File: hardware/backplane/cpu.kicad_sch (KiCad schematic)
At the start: 0 parts

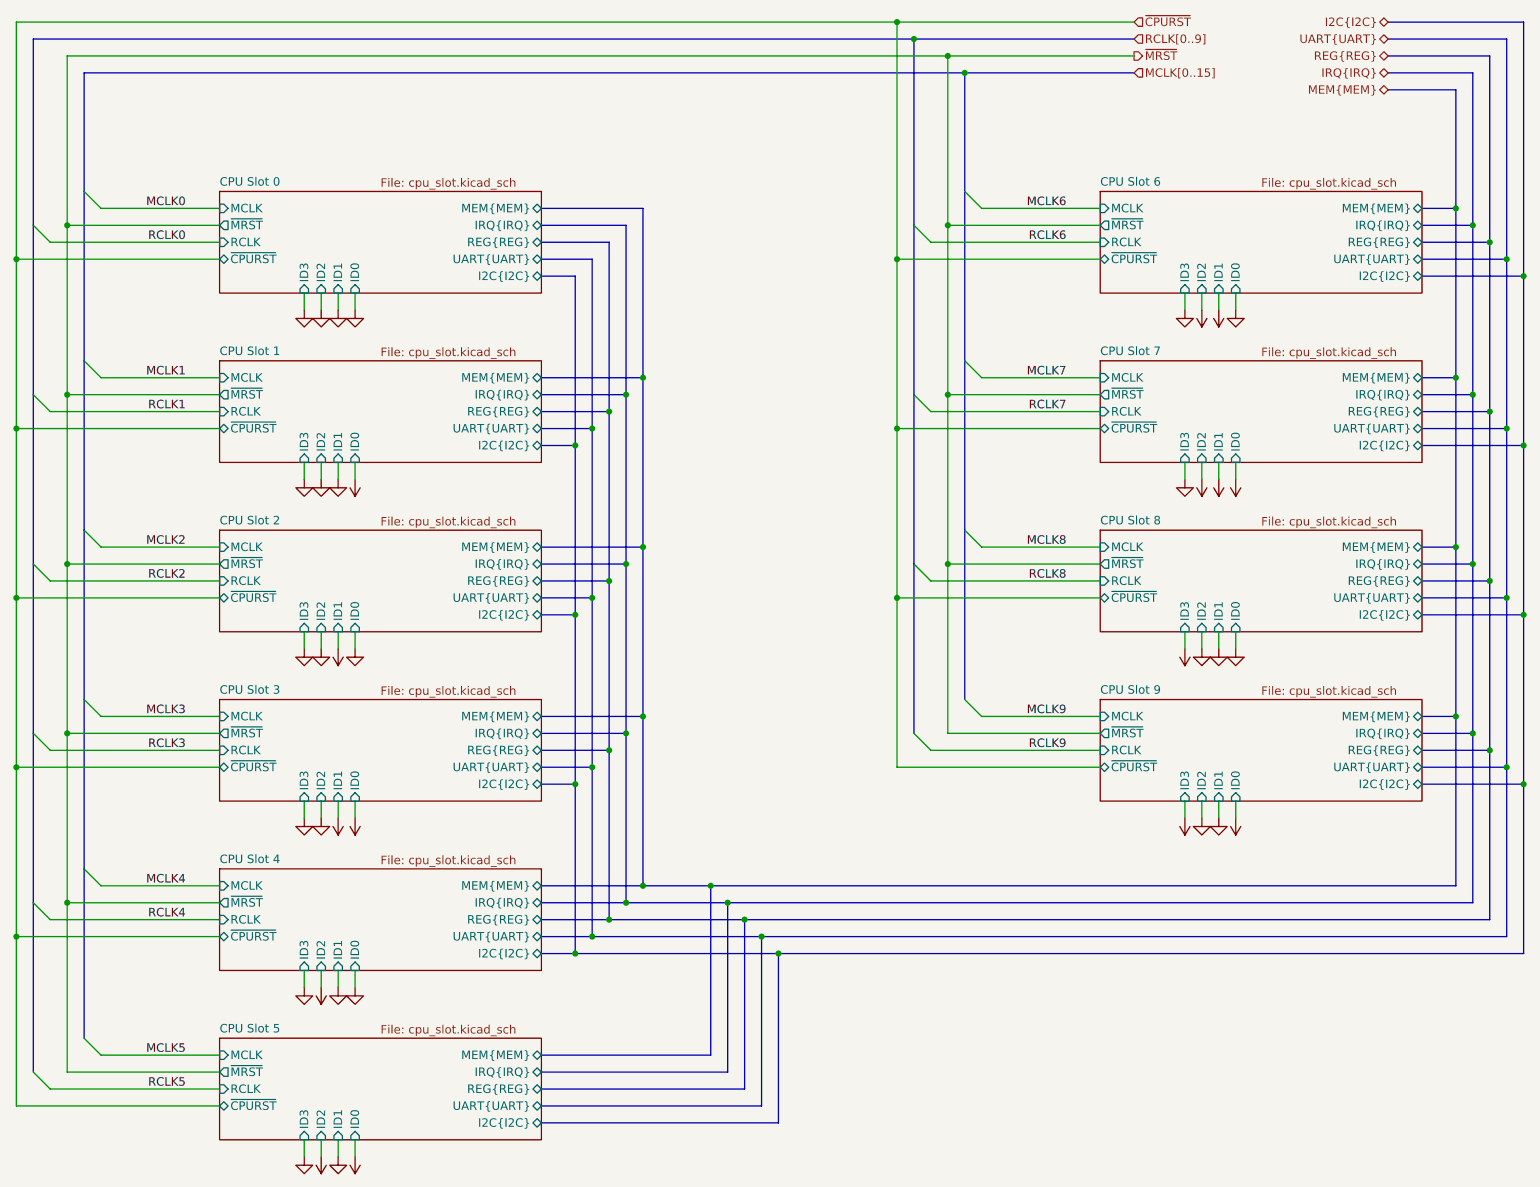
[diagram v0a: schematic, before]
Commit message: feat: Re-add peripheral MCLK, add to memory lines (#3)
Need MCLK to maintain peripheral synchronization.  Add missing memory
access size and latch lines.
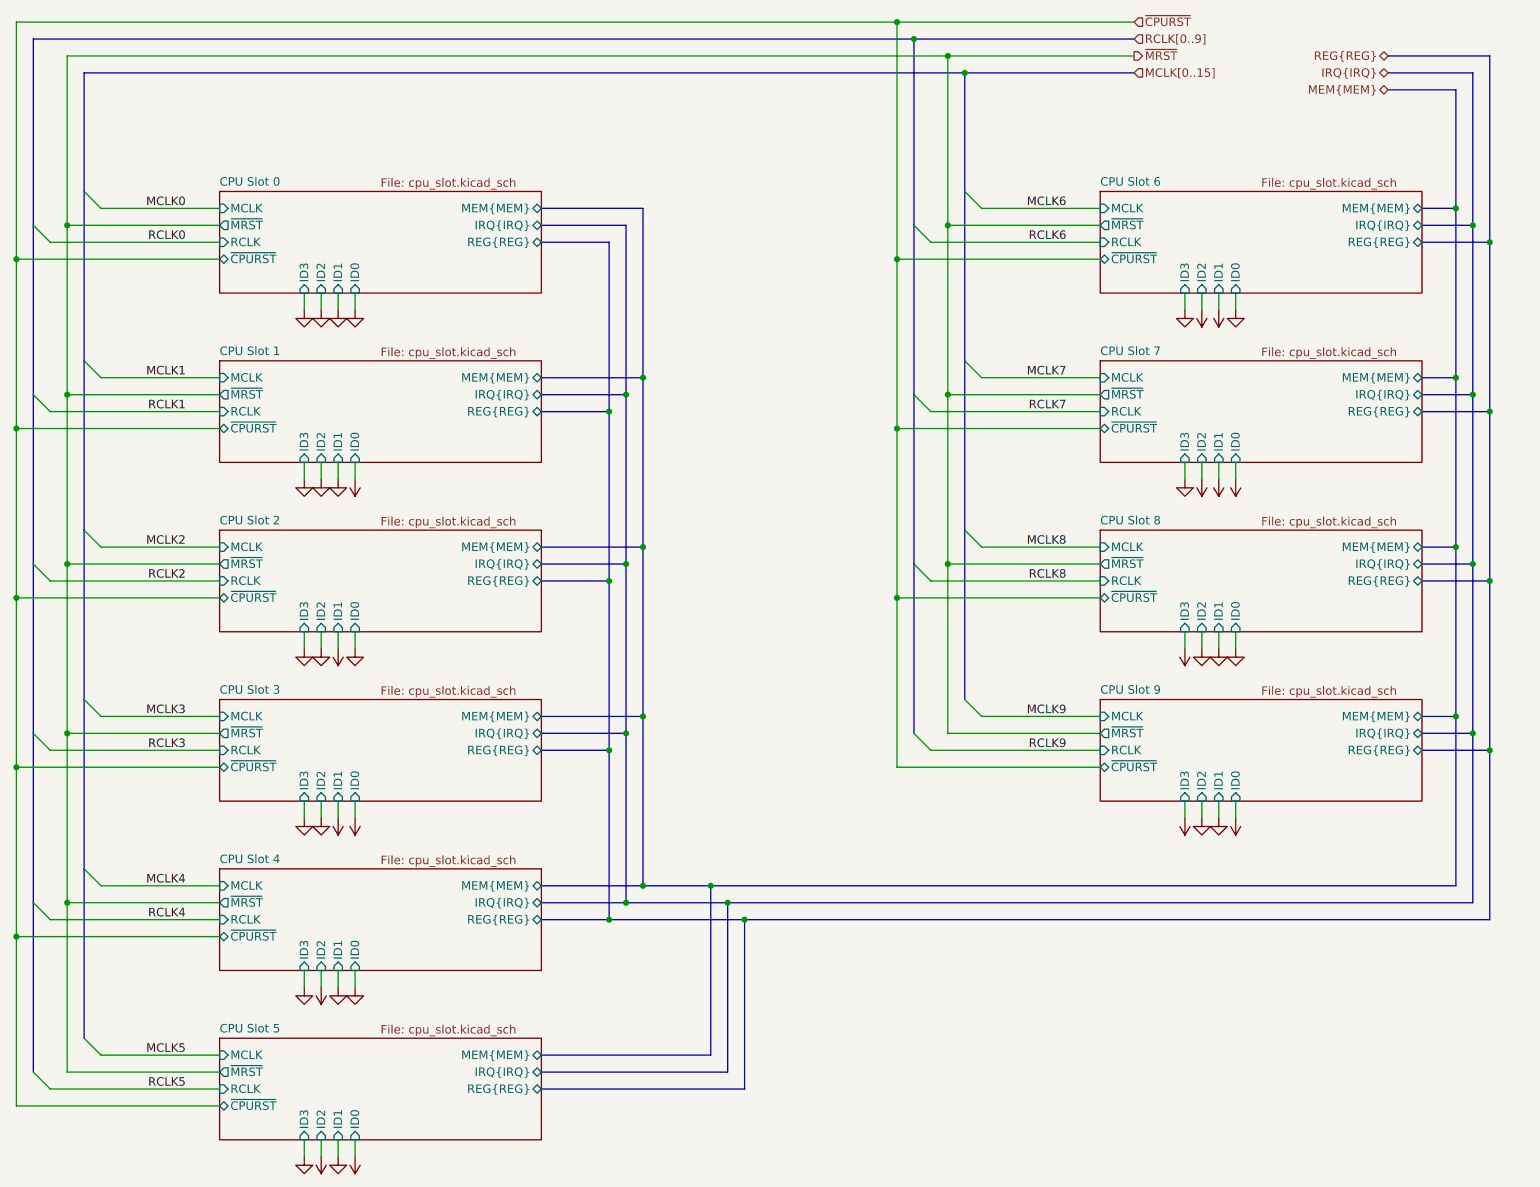
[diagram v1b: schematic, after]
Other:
- sheet CPU Slot 0 ports: added none; removed I2C{I2C}, UART{UART}
- sheet CPU Slot 1 ports: added none; removed I2C{I2C}, UART{UART}
- sheet CPU Slot 2 ports: added none; removed I2C{I2C}, UART{UART}
- sheet CPU Slot 3 ports: added none; removed I2C{I2C}, UART{UART}
- sheet CPU Slot 4 ports: added none; removed I2C{I2C}, UART{UART}
- sheet CPU Slot 5 ports: added none; removed I2C{I2C}, UART{UART}
- sheet CPU Slot 6 ports: added none; removed I2C{I2C}, UART{UART}
- sheet CPU Slot 7 ports: added none; removed I2C{I2C}, UART{UART}
- sheet CPU Slot 8 ports: added none; removed I2C{I2C}, UART{UART}
- sheet CPU Slot 9 ports: added none; removed I2C{I2C}, UART{UART}

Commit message: feat: Apply bus arch changes to backplane schematic
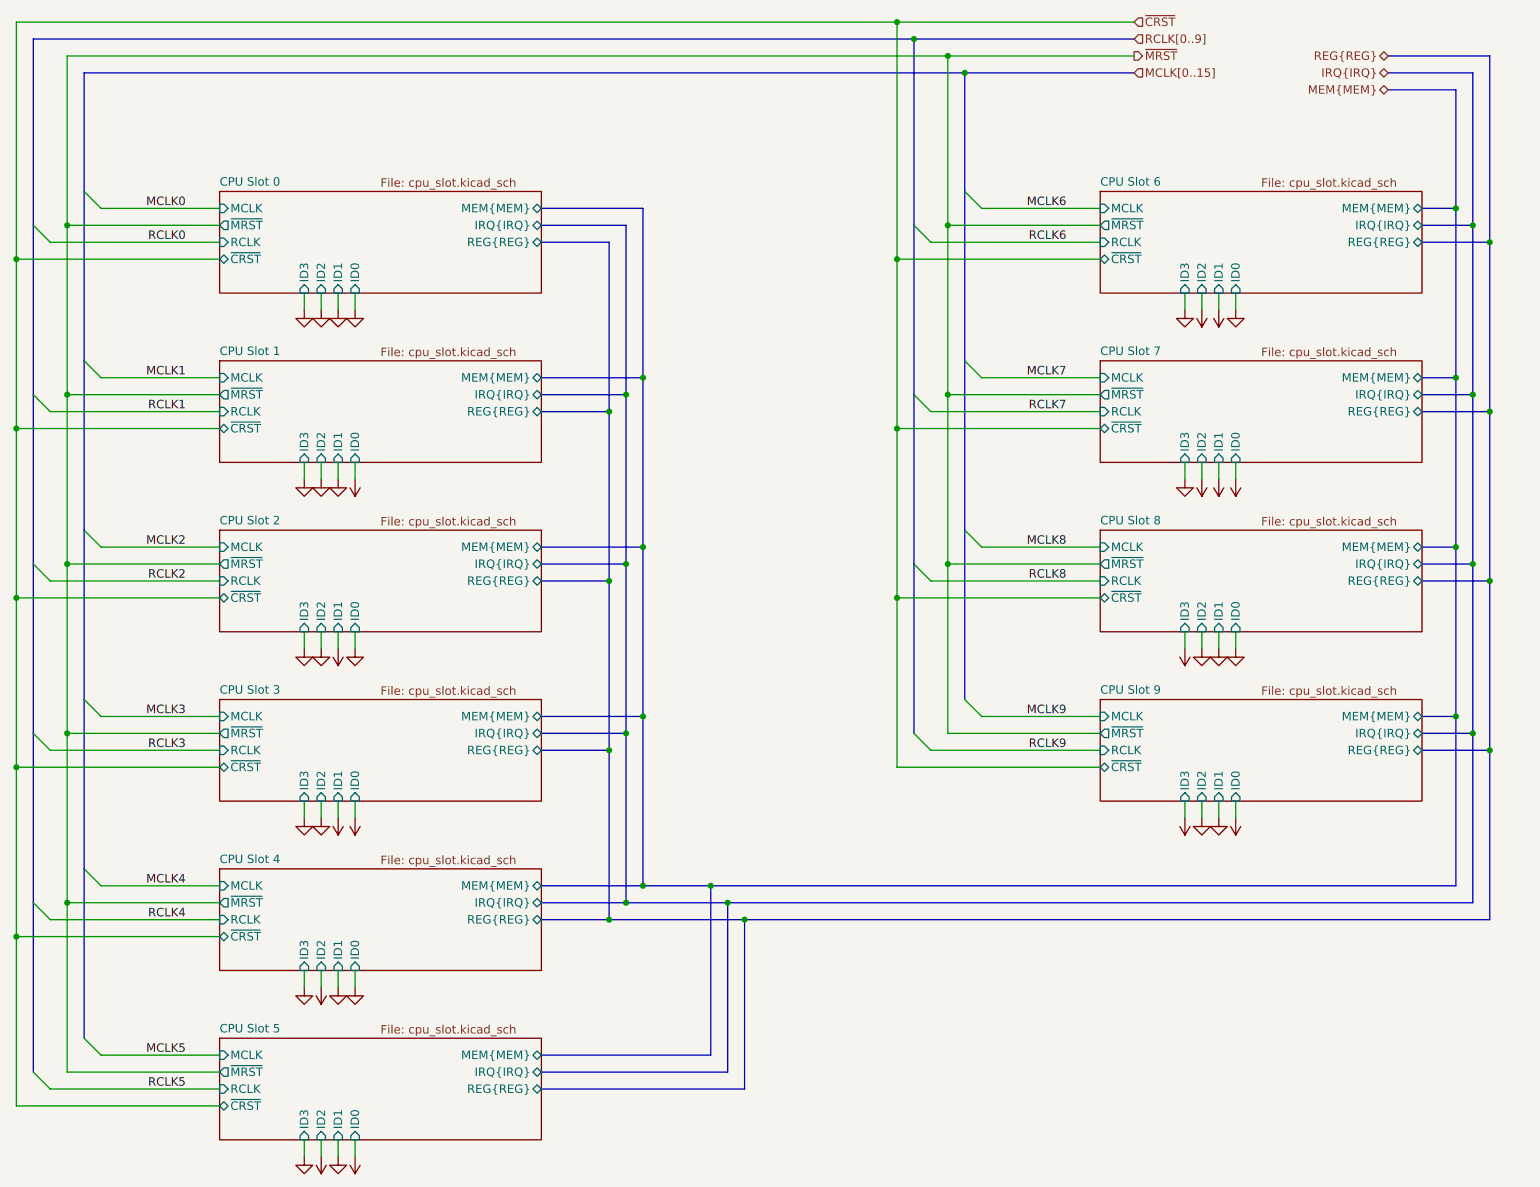
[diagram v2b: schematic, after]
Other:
- sheet CPU Slot 0 ports: added ~{CRST}; removed ~{CPURST}
- sheet CPU Slot 1 ports: added ~{CRST}; removed ~{CPURST}
- sheet CPU Slot 2 ports: added ~{CRST}; removed ~{CPURST}
- sheet CPU Slot 3 ports: added ~{CRST}; removed ~{CPURST}
- sheet CPU Slot 4 ports: added ~{CRST}; removed ~{CPURST}
- sheet CPU Slot 5 ports: added ~{CRST}; removed ~{CPURST}
- sheet CPU Slot 6 ports: added ~{CRST}; removed ~{CPURST}
- sheet CPU Slot 7 ports: added ~{CRST}; removed ~{CPURST}
- sheet CPU Slot 8 ports: added ~{CRST}; removed ~{CPURST}
- sheet CPU Slot 9 ports: added ~{CRST}; removed ~{CPURST}
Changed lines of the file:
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@@
 		)
 	)
-	(hierarchical_label "~{CPURST}"
+	(hierarchical_label "~{CRST}"
 		(shape input)
 		(at 196.85 20.32 0)
@@
 			)
 		)
-		(pin "~{CPURST}" bidirectional
+		(pin "~{CRST}" bidirectional
 			(at 59.69 157.48 180)
 			(effects
@@
 			)
 		)
-		(pin "~{CPURST}" bidirectional
+		(pin "~{CRST}" bidirectional
 			(at 59.69 182.88 180)
 			(effects
@@
 			)
 		)
-		(pin "~{CPURST}" bidirectional
+		(pin "~{CRST}" bidirectional
 			(at 59.69 132.08 180)
 			(effects
@@
 			)
 		)
-		(pin "~{CPURST}" bidirectional
+		(pin "~{CRST}" bidirectional
 			(at 191.77 81.28 180)
 			(effects
@@
 			)
 		)
-		(pin "~{CPURST}" bidirectional
+		(pin "~{CRST}" bidirectional
 			(at 191.77 106.68 180)
 			(effects
@@
 			)
 		)
-		(pin "~{CPURST}" bidirectional
+		(pin "~{CRST}" bidirectional
 			(at 191.77 55.88 180)
 			(effects
@@
 			)
 		)
-		(pin "~{CPURST}" bidirectional
+		(pin "~{CRST}" bidirectional
 			(at 59.69 55.88 180)
 			(effects
@@
 			)
 		)
-		(pin "~{CPURST}" bidirectional
+		(pin "~{CRST}" bidirectional
 			(at 59.69 81.28 180)
 			(effects
@@
 			)
 		)
-		(pin "~{CPURST}" bidirectional
+		(pin "~{CRST}" bidirectional
 			(at 59.69 106.68 180)
 			(effects
@@
 			)
 		)
-		(pin "~{CPURST}" bidirectional
+		(pin "~{CRST}" bidirectional
 			(at 191.77 132.08 180)
 			(effects
